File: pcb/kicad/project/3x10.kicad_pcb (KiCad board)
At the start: 2 copper layers, 189 x 56 mm, 72 parts, among them U1 ProMicro

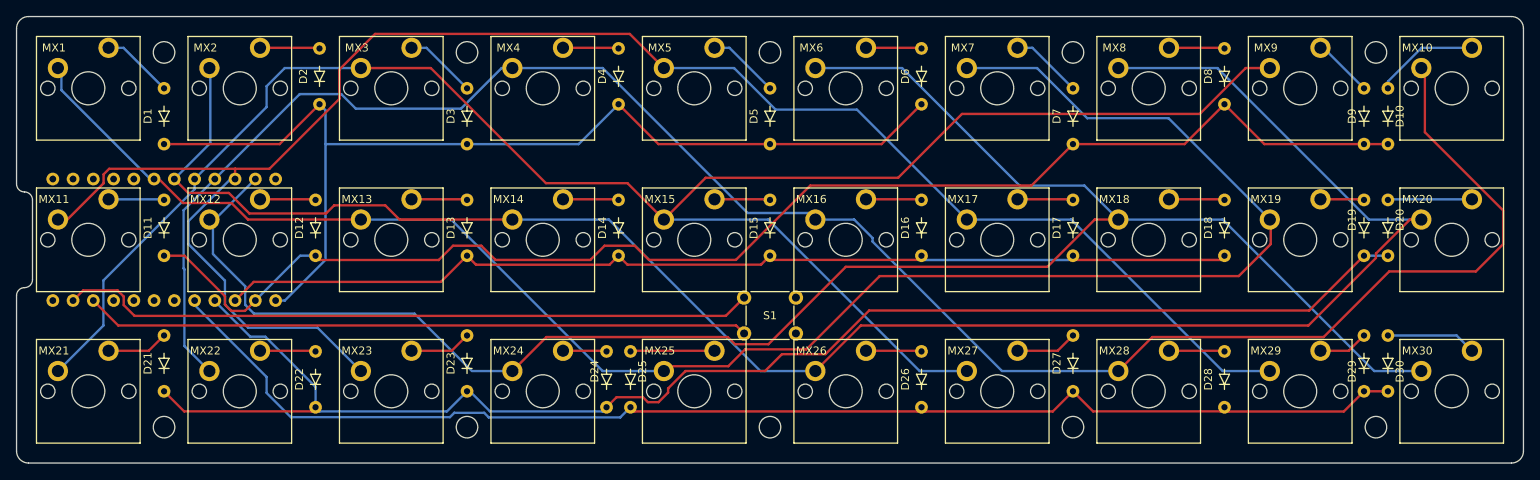
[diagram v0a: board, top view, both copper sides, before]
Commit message: 0.8mmのトレースに変更、不要なKiCadファイルの削除、ガーバー再作成
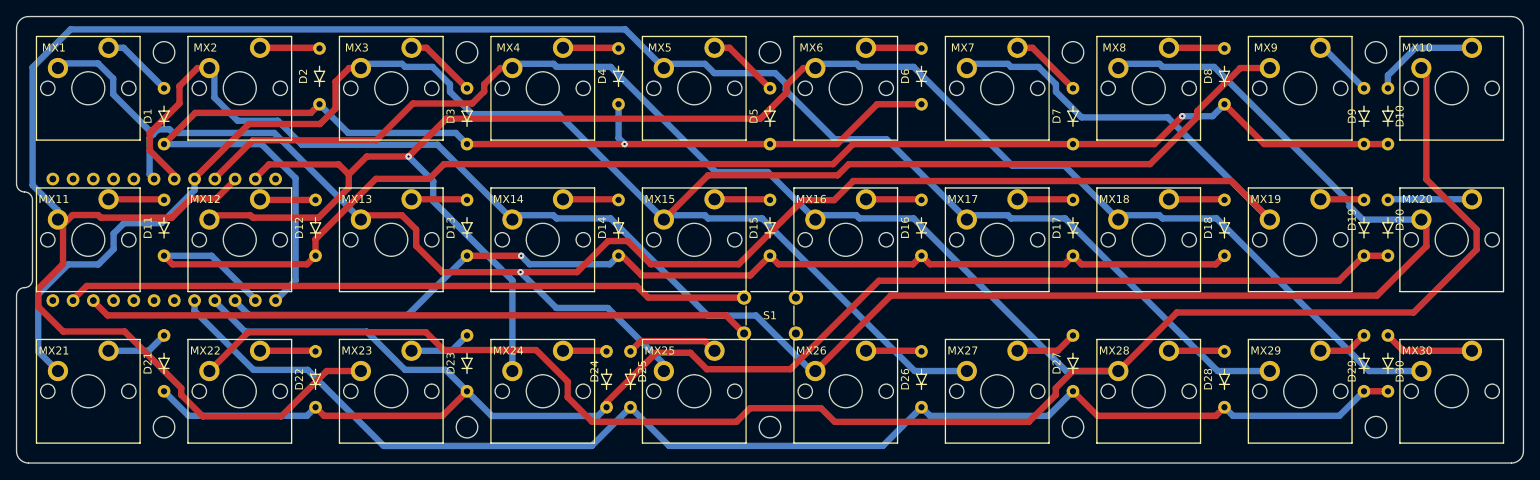
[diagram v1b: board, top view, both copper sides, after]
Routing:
- net D6(PD7): track 244.8 -> 339.5 mm
- net D7(PE6): track 224.1 -> 282.4 mm
- net D3(PD0): track 224.8 -> 252.0 mm, vias 0 -> 1
- net SCK(PB1): track 185.7 -> 205.0 mm
- net D10(PB6): track 130.7 -> 141.2 mm, vias 0 -> 1
- net D8(PB4): track 233.7 -> 223.6 mm, vias 0 -> 1
- net D4(PD4): track 237.1 -> 246.5 mm
- net D5(PC6): track 234.9 -> 244.3 mm
- net A0(PF7): track 162.5 -> 169.2 mm
- net MOSI(PB2): track 173.2 -> 179.4 mm, vias 0 -> 1
- net MISO(PB3): track 129.6 -> 133.6 mm, vias 0 -> 1
- net Net-(S1-Pad1): track 87.6 -> 85.6 mm
- net Net-(D25-Pad1): track 10.6 -> 11.6 mm
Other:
- net class 6 added: clearance 0.3, trace_width 0.6, via_dia 0.8, via_drill 0.3
- net class 8 added: clearance 0.4, trace_width 0.8, via_dia 0.8, via_drill 0.3
- net class Default: clearance 0.25 -> 0.2; via_drill 0.4 -> 0.3
- rule trace_clearance: 0.25 -> 0.2
- rule via_min_size: 0.4 -> 0.8
